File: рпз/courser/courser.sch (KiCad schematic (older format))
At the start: 7 parts

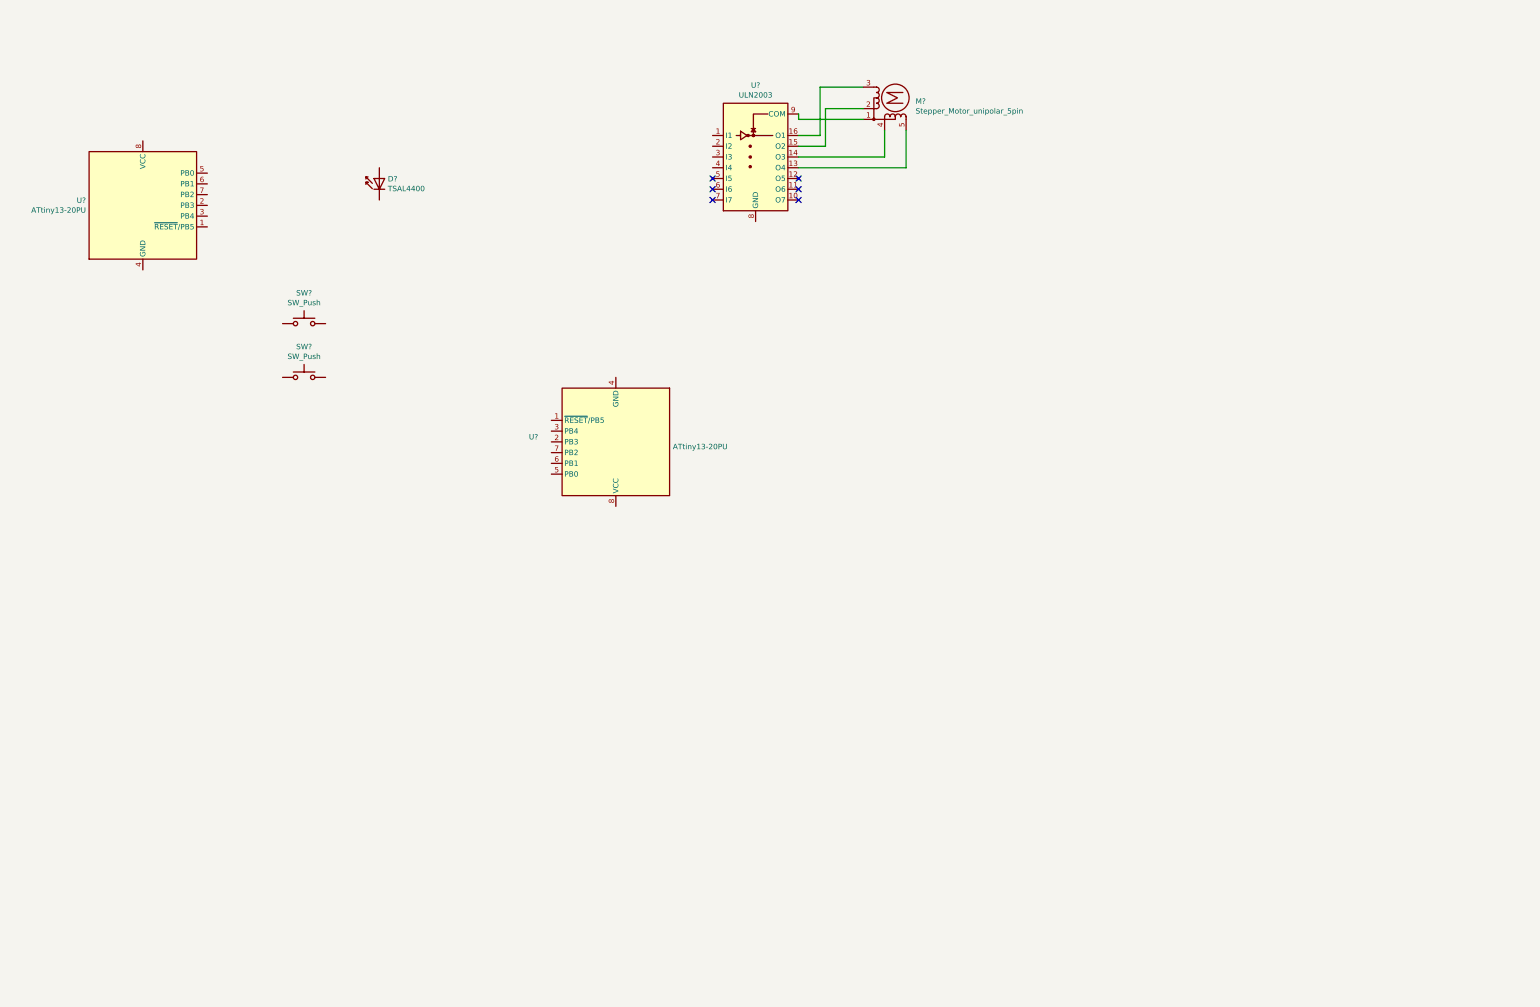
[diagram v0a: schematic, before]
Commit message: master and slave for one pulse
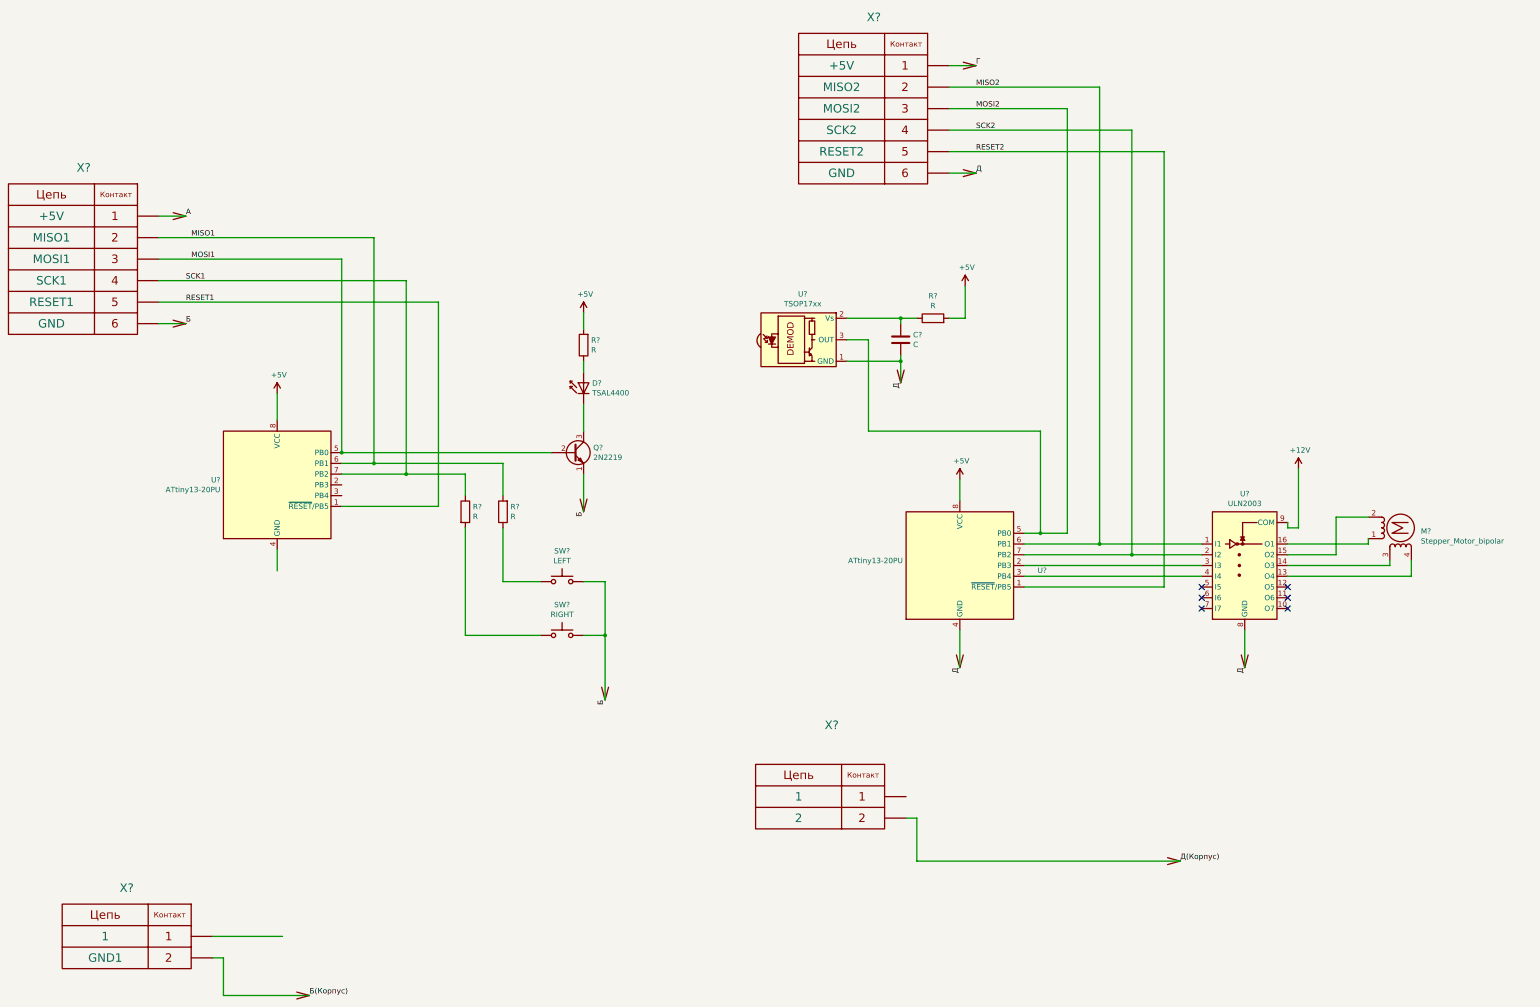
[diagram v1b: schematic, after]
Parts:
- removed M?: Stepper_Motor_unipolar_5pin, symbol Motor:Stepper_Motor_unipolar_5pin
- added C?: C, symbol Device:C
- added M?: Stepper_Motor_bipolar, symbol Motor:Stepper_Motor_bipolar
- added Q?: 2N2219, Package_TO_SOT_THT:TO-39-3, symbol Transistor_BJT:2N2219
- added R? (x4): R, symbol Device:R
- added U?: TSOP17xx, OptoDevice:Vishay_CAST-3Pin, symbol Interface_Optical:TSOP17xx
- added X? (x2): CONN_6, symbol Connector_Generic_GOST:CONN_6
- added X? (x2): CONN_2, symbol Connector_Generic_GOST:CONN_2
- SW?: value SW_Push -> LEFT
- SW?: value SW_Push -> RIGHT
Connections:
- net RESET1: now reaches U?.1 (~RESET~/PB5)
- net RESET1: now also X?.5
- net MOSI1: now reaches U?.5 (PB0)
- net MOSI1: now also Q?.2 (B), X?.3
- net MISO1: now reaches U?.6 (PB1)
- net MISO1: now also R?.2, X?.2
- net SCK1: now reaches U?.7 (PB2)
- net SCK1: now also R?.1, X?.4
- net +5V: now reaches U?.8 (VCC)
- net +5V: now also U?.8 (VCC), R?.2, R?.2
- net RESET2: now reaches U?.1 (~RESET~/PB5)
- net RESET2: now also X?.5
- net at U?.2 (PB3): now also U?.3 (I3)
- net at U?.3 (PB4): now also U?.4 (I4)
- net Д: now reaches U?.4 (GND)
- net Д: now also U?.8 (GND), C?.2, U?.1 (GND), X?.6
- net MOSI2: now reaches U?.5 (PB0)
- net MOSI2: now also U?.3 (OUT), X?.3
- net MISO2: now reaches U?.6 (PB1)
- net MISO2: now also U?.1 (I1), X?.2
- net SCK2: now reaches U?.7 (PB2)
- net SCK2: now also U?.2 (I2), X?.4
- net at SW?.1: now also R?.1
- net Б: now reaches SW?.2
- net Б: now also SW?.2, Q?.1 (E), X?.6
- net at SW?.1: now also R?.2
- net at D?.1 (K): now also Q?.3 (C)
- net at D?.2 (A): now also R?.1
- net at U?.13 (O4): now also M?.4
- net at U?.14 (O3): now also M?.3
- net at U?.15 (O2): now also M?.2 (-)
- net at U?.16 (O1): now also M?.1
- net +12V: now reaches U?.9 (COM)
- new net: C?.1, R?.1, U?.2 (Vs)
- new net A: X?.1
- new net Б(Корпус): X?.2
- new net Г: X?.1
- new net Д(Корпус): X?.2
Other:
- moved on the sheet: D?, SW?, U?
